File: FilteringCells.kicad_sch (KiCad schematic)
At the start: 3 parts

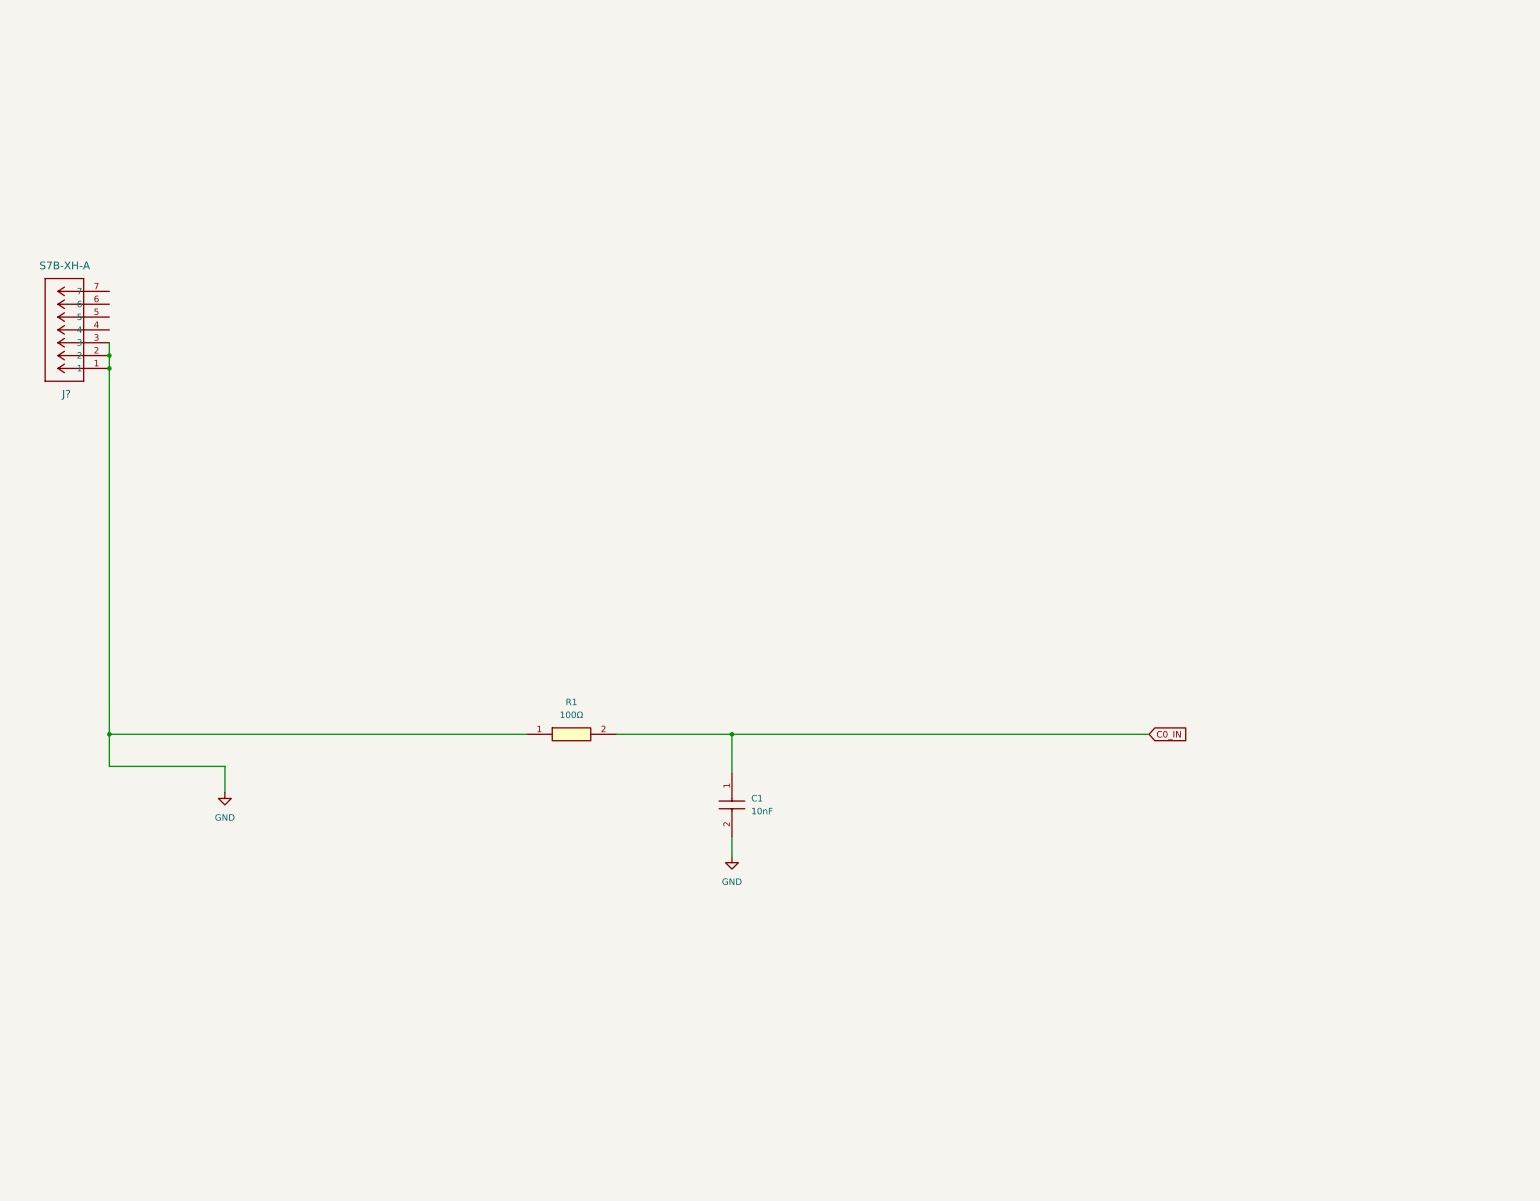
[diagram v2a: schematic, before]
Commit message: feat: add filtering circuit
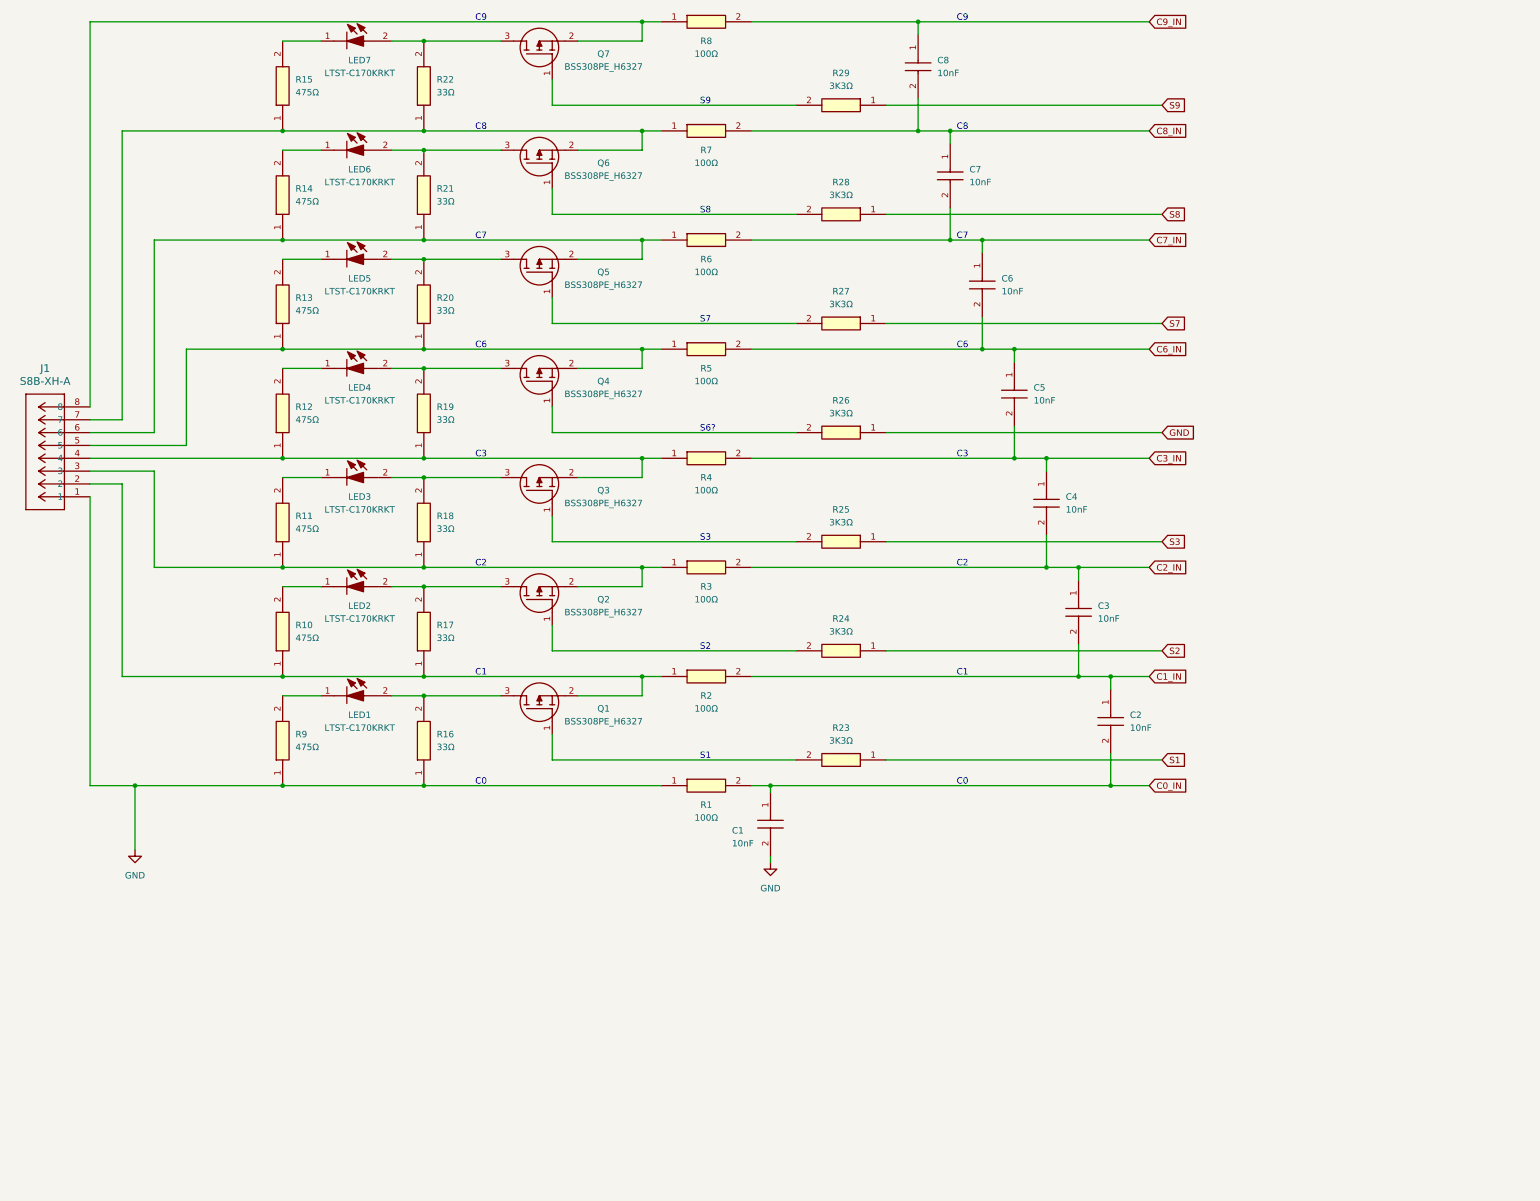
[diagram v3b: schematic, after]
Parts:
- removed J?: S7B-XH-A, CONN_S7B-XH-A_JST, symbol FixedWing:S7B-XH-A
- added C2, C3, C4, C5, C6, C7, C8: 10nF, CAPC2012X95N, symbol FixedWing:AC0805KRX7R8BB103
- added J1: S8B-XH-A, CONN_S8B-XH-A_JST, symbol FixedWing:S8B-XH-A
- added LED1, LED2, LED3, LED4, LED5, LED6, LED7: LTST-C170KRKT, LEDC2012X120N, symbol FixedWing:LTST-C170KRKT
- added Q1, Q2, Q3, Q4, Q5, Q6, Q7: BSS308PE_H6327, SOT95P260X110-3N, symbol FixedWing:BSS308PE_H6327
- added R10, R11, R12, R13, R14, R15, R9: 475Ω, RESC2012X50N, symbol FixedWing:CRCW0805475RFKEA
- added R16, R17, R18, R19, R20, R21, R22: 33Ω, RESC6332X70N, symbol FixedWing:CRCW251233R0FKEG
- added R2, R3, R4, R5, R6, R7, R8: 100Ω, RESC2012X50N, symbol FixedWing:CRCW0805100RFKEA
- added R23, R24, R25, R26, R27, R28, R29: 3K3Ω, RESC2012X50N, symbol FixedWing:CRCW08053K30JNEA
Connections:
- net C0_IN: now also C2.2
- net GND: now also J1.1, R16.1, R26.1, R9.1
- new net: J1.2, Q1.2 (S), R10.1, R17.1, R2.1
- new net: LED2.2 (A), Q2.3 (D), R17.2
- new net: Q2.1 (G), R24.2
- new net: J1.3, Q2.2 (S), R11.1, R18.1, R3.1
- new net: Q4.1 (G), R26.2
- new net: LED4.1 (K), R12.2
- new net: LED4.2 (A), Q4.3 (D), R19.2
- new net: J1.7, Q6.2 (S), R15.1, R22.1, R7.1
- new net: LED7.1 (K), R15.2
- new net: Q1.1 (G), R23.2
- new net: LED1.2 (A), Q1.3 (D), R16.2
- new net: LED2.1 (K), R10.2
- new net: Q7.1 (G), R29.2
- new net: J1.5, Q4.2 (S), R13.1, R20.1, R5.1
- new net: LED5.1 (K), R13.2
- new net: LED1.1 (K), R9.2
- new net: J1.6, Q5.2 (S), R14.1, R21.1, R6.1
- new net: LED6.1 (K), R14.2
- new net: Q3.1 (G), R25.2
- new net: LED6.2 (A), Q6.3 (D), R21.2
- new net: J1.4, Q3.2 (S), R12.1, R19.1, R4.1
- new net: Q5.1 (G), R27.2
- new net: Q6.1 (G), R28.2
- new net: LED7.2 (A), Q7.3 (D), R22.2
- new net: LED3.2 (A), Q3.3 (D), R18.2
- new net: LED5.2 (A), Q5.3 (D), R20.2
- new net: J1.8, Q7.2 (S), R8.1
- new net: LED3.1 (K), R11.2
- new net C1_IN: C2.1, C3.2, R2.2
- new net C2_IN: C3.1, C4.2, R3.2
- new net C3_IN: C4.1, C5.2, R4.2
- new net C6_IN: C5.1, C6.2, R5.2
- new net C7_IN: C6.1, C7.2, R6.2
- new net C8_IN: C7.1, C8.2, R7.2
- new net C9_IN: C8.1, R8.2
- new net S1: R23.1
- new net S2: R24.1
- new net S3: R25.1
- new net S7: R27.1
- new net S8: R28.1
- new net S9: R29.1
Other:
- note added: "C0"
- note added: "C1"
- note added: "C2"
- note added: "C3"
- note added: "C6"
- note added: "C7"
- note added: "C8"
- note added: "C9"
- note added: "S1"
- note added: "S2"
- note added: "S3"
- note added: "S6?"
- note added: "S7"
- note added: "S8"
- note added: "S9"
- company: (none) -> AeroNU FixedWing
- title: (none) -> BMS Cell Filtering Logic
- moved on the sheet: C1, R1

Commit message: feat: resolved splitting cells across monitor
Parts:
- removed C5: 10nF, CAPC2012X95N, symbol FixedWing:AC0805KRX7R8BB103
- removed J1: S8B-XH-A, CONN_S8B-XH-A_JST, symbol FixedWing:S8B-XH-A
- removed LED4: LTST-C170KRKT, LEDC2012X120N, symbol FixedWing:LTST-C170KRKT
- removed Q4: BSS308PE_H6327, SOT95P260X110-3N, symbol FixedWing:BSS308PE_H6327
- removed R12: 475Ω, RESC2012X50N, symbol FixedWing:CRCW0805475RFKEA
- removed R19: 33Ω, RESC6332X70N, symbol FixedWing:CRCW251233R0FKEG
- removed R26: 3K3Ω, RESC2012X50N, symbol FixedWing:CRCW08053K30JNEA
- added J1: S7B-XH-A, CONN_S7B-XH-A_JST, symbol FixedWing:S7B-XH-A
- added R12, R19: 100Ω, RESC2012X50N, symbol FixedWing:CRCW0805100RFKEA
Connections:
- net GND: now also J1.1
- net at Q1.2 (S), R10.1, R17.1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: now also J1.2
- net at Q2.2 (S), R11.1, R18.1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: now also J1.3
- net at Q6.2 (S), R15.1, R22.1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: now also J1.6
- net at R13.1, R20.1, R5.1: now also Q3.2 (S), R4.1, J1.4
- net at Q5.2 (S), R14.1, R21.1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: now also J1.5
- net at Q7.2 (S), R8.1: now also J1.7, R12.1, R19.1
- net C0_IN renamed C0
- net C1_IN renamed C1
- net C2_IN renamed C2
- net C3_IN renamed C3
- net C3: now also C6.2
- net C6_IN renamed C6
- net C6: no longer C6.2
- net C7_IN renamed C7
- net C8_IN renamed C8
- net C9_IN renamed C9
- new net C12: R12.2
- new net VIN_MONITOR: R19.2
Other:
- note removed: "S6?"
- moved on the sheet: C1, C2, C3, C4, C6, C7, C8, LED1, LED2, LED3, LED5, LED6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
